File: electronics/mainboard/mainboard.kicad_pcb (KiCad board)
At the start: 2 copper layers, 43.7 x 137 mm, 24 parts, among them Q1 TSM250N02CX_RFG, Q2 TSM250N02CX_RFG, SW1 SW_Push, SW10 SW_Push, SW11 SW_Push, SW12 SW_Push, SW13 SW_Push, SW14 SW_Push, SW15 SW_Push, SW2 SW_Push, SW3 SW_Push, SW4 SW_Push, SW5 SW_Push, SW6 SW_Push, SW7 SW_Push, SW8 SW_Push, SW9 SW_Push, U1 1022

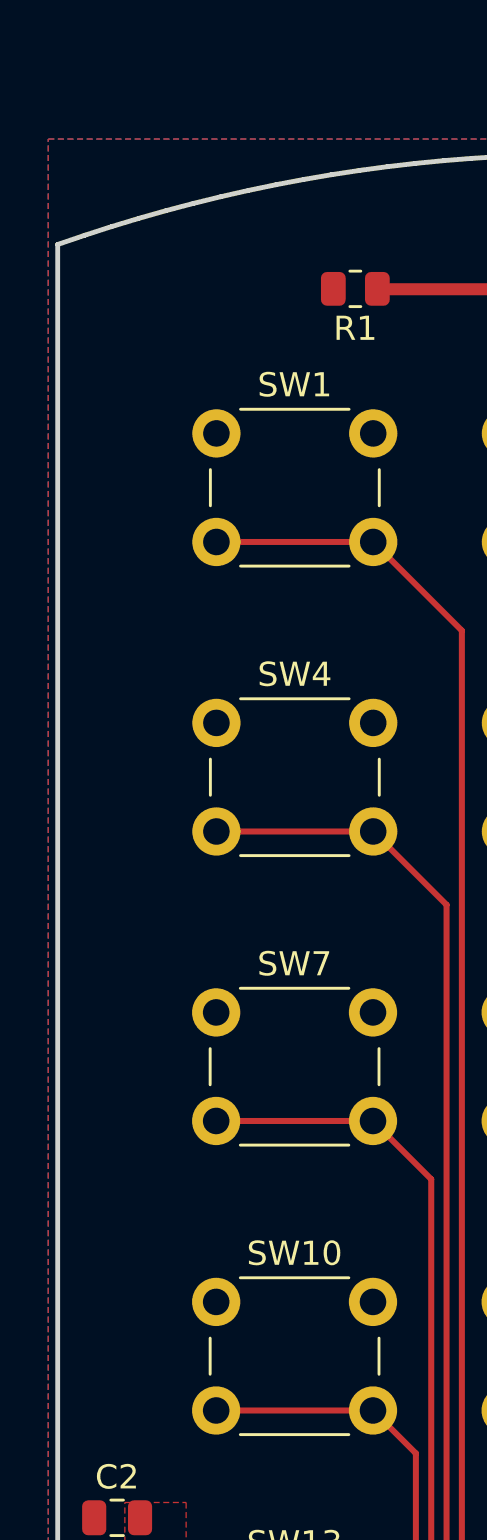
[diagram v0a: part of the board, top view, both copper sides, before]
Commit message: add informations about project and version
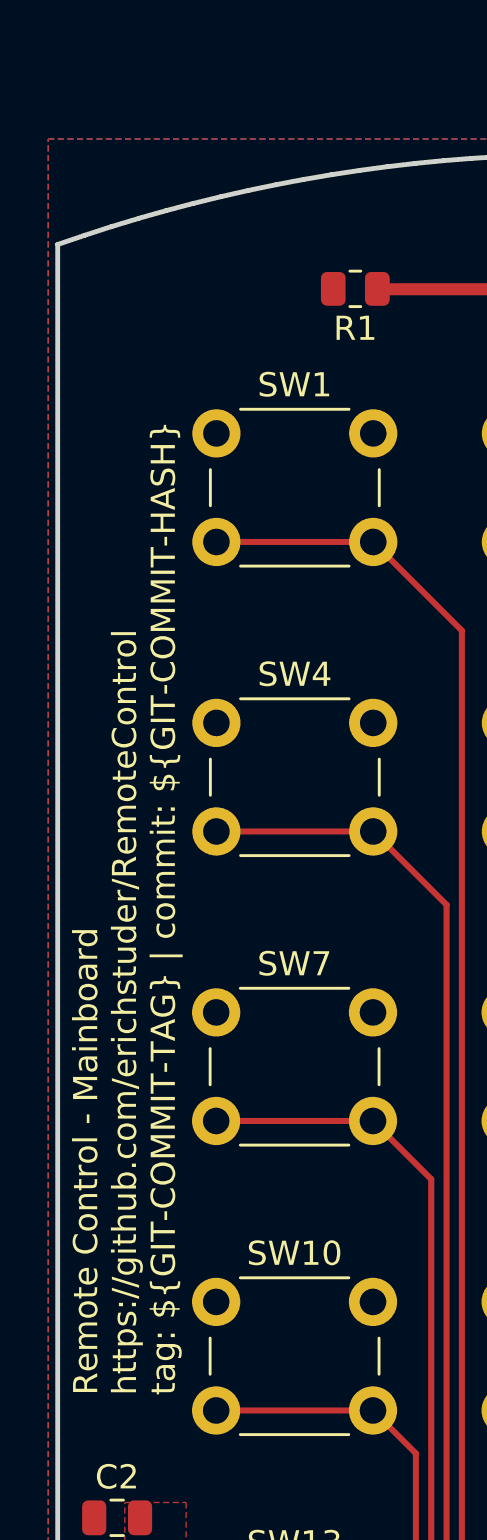
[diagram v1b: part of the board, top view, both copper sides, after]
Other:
- board text added: "Remote Control - Mainboard https://github.com/erichstuder/RemoteControl tag: ${GIT-COMMIT-TAG} | commit: ${GIT-COMMIT-HASH}"
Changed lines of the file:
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@@
   )
   (setup
+    (stackup
+      (layer "F.SilkS" (type "Top Silk Screen"))
+      (layer "F.Paste" (type "Top Solder Paste"))
+      (layer "F.Mask" (type "Top Solder Mask") (thickness 0.01))
+      (layer "F.Cu" (type "copper") (thickness 0.035))
+      (layer "dielectric 1" (type "core") (thickness 1.51) (material "FR4") (epsilon_r 4.5) (loss_tangent 0.02))
+      (layer "B.Cu" (type "copper") (thickness 0.035))
+      (layer "B.Mask" (type "Bottom Solder Mask") (thickness 0.01))
+      (layer "B.Paste" (type "Bottom Solder Paste"))
+      (layer "B.SilkS" (type "Bottom Silk Screen"))
+      (copper_finish "None")
+      (dielectric_constraints no)
+    )
     (pad_to_mask_clearance 0)
     (grid_origin 110.2471 44.0637)
@@
     )
   )
+  (property "GIT-COMMIT-HASH" "noHash")
+  (property "GIT-COMMIT-TAG" "noTag")
   (net 0 "")
   (net 1 "unconnected-(A1-Pad3)")
@@
   (gr_line (start 121.3867 122.2996) (end 121.3654 122.2844) (layer "Edge.Cuts") (width 0.2))
   (gr_line (start 122.2994 119.5718) (end 122.3256 119.57294) (layer "Edge.Cuts") (width 0.2))
+  (gr_text "Remote Control - Mainboard\nhttps://github.com/erichstuder/RemoteControl\ntag: ${GIT-COMMIT-TAG} | commit: ${GIT-COMMIT-HASH}" (at 91.1971 95.4987 90) (layer "F.SilkS")
+    (effects (font (size 1 1) (thickness 0.15)) (justify left))
+  )
   (segment (start 101.67996 49.655) (end 108.9727 49.655) (width 0.5) (layer "F.Cu") (net 11))
   (segment (start 101.663509 49.638549) (end 101.67996 49.655) (width 0.25) (layer "F.Cu") (net 11))

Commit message: modify project informations
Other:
- board text added: "${PROJECT} ${PROJECT-URL} tag: ${GIT-COMMIT-TAG} | commit: ${GIT-COMMIT-HASH}"
- board text removed: "Remote Control - Mainboard https://github.com/erichstuder/RemoteControl tag: ${GIT-COMMIT-TAG} | commit: ${GIT-COMMIT-HASH}"
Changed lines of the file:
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@@
   (property "GIT-COMMIT-HASH" "noHash")
   (property "GIT-COMMIT-TAG" "noTag")
+  (property "PROJECT" "Remote Control - Mainboard")
+  (property "PROJECT-URL" "https://github.com/erichstuder/RemoteControl")
   (net 0 "")
   (net 1 "unconnected-(A1-Pad3)")
@@
   (gr_line (start 121.3867 122.2996) (end 121.3654 122.2844) (layer "Edge.Cuts") (width 0.2))
   (gr_line (start 122.2994 119.5718) (end 122.3256 119.57294) (layer "Edge.Cuts") (width 0.2))
-  (gr_text "Remote Control - Mainboard\nhttps://github.com/erichstuder/RemoteControl\ntag: ${GIT-COMMIT-TAG} | commit: ${GIT-COMMIT-HASH}" (at 91.1971 95.4987 90) (layer "F.SilkS")
+  (gr_text "${PROJECT}\n${PROJECT-URL}\ntag: ${GIT-COMMIT-TAG} | commit: ${GIT-COMMIT-HASH}" (at 91.1971 95.4987 90) (layer "F.SilkS")
     (effects (font (size 1 1) (thickness 0.15)) (justify left))
   )
